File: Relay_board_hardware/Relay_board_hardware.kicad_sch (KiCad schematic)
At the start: 18 parts, among them IC1 BTS3800SL, Q1 IRF740ASPBF, U1 AD8541, U2 MCP1416

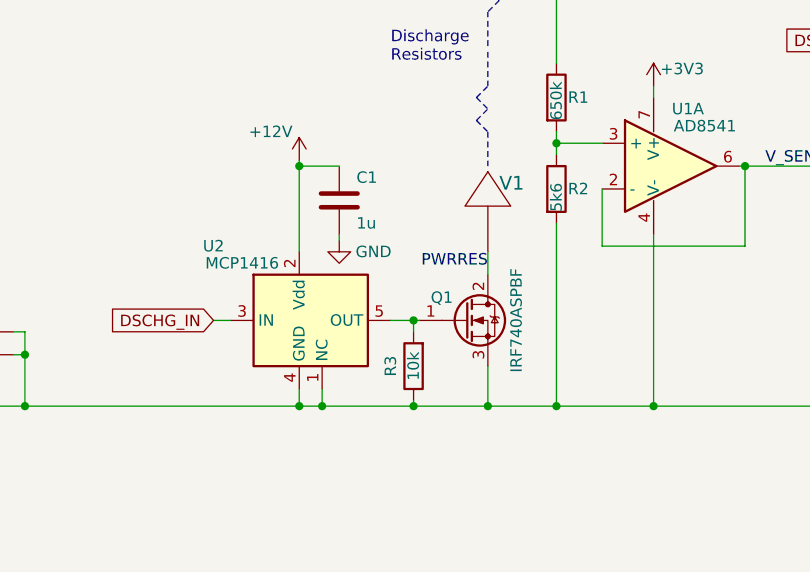
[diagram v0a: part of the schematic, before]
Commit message: added filter cap, changed opamp datasheet
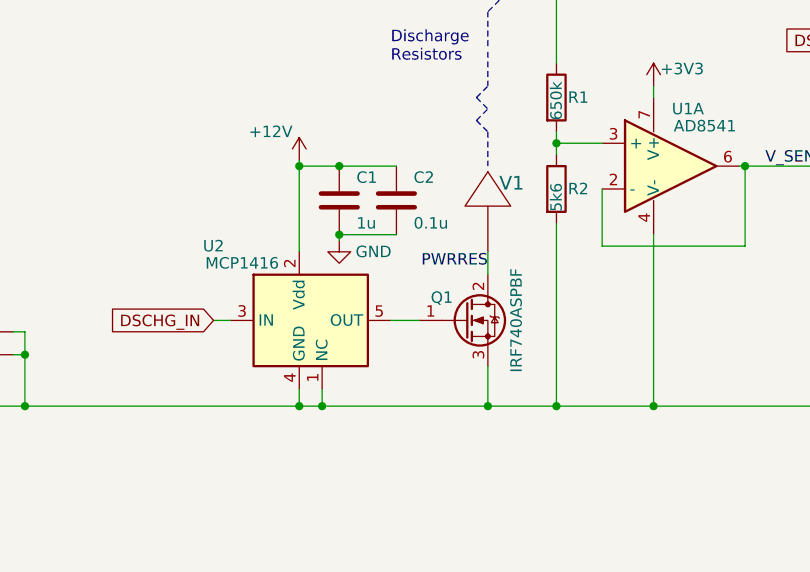
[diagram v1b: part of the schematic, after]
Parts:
- removed R3: 10k, Resistor_SMD:R_0603_1608Metric_Pad0.98x0.95mm_HandSolder, symbol Device:R
- added C2: 0.1u, Capacitor_SMD:C_0603_1608Metric_Pad1.08x0.95mm_HandSolder, symbol Device:C
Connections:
- net +12V: now also C2.1
- net GND: now also C2.2
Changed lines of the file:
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@@
   (junction (at 114.935 83.82) (diameter 0) (color 0 0 0 0)
   )
-  (junction (at 158.115 80.01) (diameter 0) (color 0 0 0 0)
-  )
   (junction (at 145.415 62.865) (diameter 0) (color 0 0 0 0)
   )
@@
   (junction (at 61.595 89.535) (diameter 0) (color 0 0 0 0)
   )
-  (junction (at 158.115 89.535) (diameter 0) (color 0 0 0 0)
-  )
   (junction (at 33.655 89.535) (diameter 0) (color 0 0 0 0)
   )
   (junction (at 184.785 89.535) (diameter 0) (color 0 0 0 0)
   )
+  (junction (at 149.86 70.485) (diameter 0) (color 0 0 0 0)
+  )
   (junction (at 114.935 89.535) (diameter 0) (color 0 0 0 0)
   )
@@
   (junction (at 147.955 89.535) (diameter 0) (color 0 0 0 0)
   )
+  (junction (at 149.86 62.865) (diameter 0) (color 0 0 0 0)
+  )
   (junction (at 46.355 54.61) (diameter 0) (color 0 0 0 0)
   )
@@
     (stroke (width 0) (type dash_dot))
   )
-  (wire (pts (xy 158.115 89.535) (xy 166.37 89.535))
-    (stroke (width 0) (type default))
-  )
   (wire (pts (xy 173.99 61.595) (xy 173.99 60.325))
     (stroke (width 0) (type default))
@@
     (stroke (width 0) (type default))
   )
-  (wire (pts (xy 158.115 88.9) (xy 158.115 89.535))
-    (stroke (width 0) (type default))
-  )
   (wire (pts (xy 179.07 71.755) (xy 194.945 71.755))
     (stroke (width 0) (type default))
   )
-  (wire (pts (xy 158.115 80.01) (xy 158.75 80.01))
-    (stroke (width 0) (type default))
-  )
   (wire (pts (xy 210.82 89.535) (xy 184.785 89.535))
     (stroke (width 0) (type default))
@@
     (stroke (width 0) (type default))
   )
-  (wire (pts (xy 158.115 80.01) (xy 158.115 81.28))
-    (stroke (width 0) (type default))
-  )
   (wire (pts (xy 38.735 57.785) (xy 38.735 44.45))
     (stroke (width 0) (type default))
@@
     (stroke (width 0) (type default))
   )
-  (wire (pts (xy 147.955 89.535) (xy 158.115 89.535))
+  (wire (pts (xy 147.955 89.535) (xy 166.37 89.535))
     (stroke (width 0) (type default))
   )
@@
     (stroke (width 0) (type default))
   )
+  (wire (pts (xy 149.86 70.485) (xy 156.21 70.485))
+    (stroke (width 0) (type default))
+  )
   (wire (pts (xy 114.935 83.82) (xy 114.935 81.28))
     (stroke (width 0) (type default))
   )
+  (wire (pts (xy 149.86 62.865) (xy 156.21 62.865))
+    (stroke (width 0) (type default))
+  )
   (wire (pts (xy 212.09 46.355) (xy 210.82 46.355))
     (stroke (width 0) (type default))
@@
     (stroke (width 0) (type default))
   )
-  (wire (pts (xy 155.575 80.01) (xy 158.115 80.01))
+  (wire (pts (xy 155.575 80.01) (xy 158.75 80.01))
     (stroke (width 0) (type default))
   )
@@
       (effects (font (size 1.27 1.27)) hide)
     )
-    (property "Datasheet" "https://www.mouser.com/ProductDetail/Microchip-Technology/MCP6497T-E-SN?qs=8Wlm6%252BaMh8Sq3ZIB9JIi0Q%3D%3D" (at 187.325 62.865 0)
+    (property "Datasheet" "https://www.digikey.com/en/products/detail/analog-devices-inc/AD8541ARZ-REEL7/996008" (at 187.325 62.865 0)
       (effects (font (size 1.27 1.27)) hide)
     )
@@
     )
   )
+  (symbol (lib_id "Device:C") (at 156.21 66.675 0) (unit 1)
+    (in_bom yes) (on_board yes) (dnp no)
+    (property "Reference" "C2" (at 158.115 64.135 0)
+      (effects (font (size 1.27 1.27)) (justify left))
+    )
+    (property "Value" "0.1u" (at 158.115 69.215 0)
+      (effects (font (size 1.27 1.27)) (justify left))
+    )
+    (property "Footprint" "Capacitor_SMD:C_0603_1608Metric_Pad1.08x0.95mm_HandSolder" (at 157.1752 70.485 0)
+      (effects (font (size 1.27 1.27)) hide)
+    )
+    (property "Datasheet" "~https://www.digikey.com/en/products/detail/yageo/CC1210KKX7R7BB105/7164418" (at 156.21 66.675 0)
+      (effects (font (size 1.27 1.27)) hide)
+    )
+    (pin "1")
+    (pin "2")
+    (instances
+      (project "Relay_board_hardware"
+        (path "/e63e39d7-6ac0-4ffd-8aa3-1841a4541b55"
+          (reference "C2") (unit 1)
+        )
+      )
+    )
+  )
   (symbol (lib_id "Device:Opamp_Dual") (at 186.69 62.865 0) (unit 1)
     (in_bom yes) (on_board yes) (dnp no)
@@
       (effects (font (size 1.27 1.27)) hide)
     )
-    (property "Datasheet" "https://www.mouser.com/ProductDetail/Microchip-Technology/MCP6497T-E-SN?qs=8Wlm6%252BaMh8Sq3ZIB9JIi0Q%3D%3D" (at 186.69 62.865 0)
+    (property "Datasheet" "https://www.digikey.com/en/products/detail/analog-devices-inc/AD8541ARZ-REEL7/996008" (at 186.69 62.865 0)
       (effects (font (size 1.27 1.27)) hide)
     )
@@
         )
       )
-    )
-  )
-  (symbol (lib_id "Device:R") (at 158.115 85.09 180) (unit 1)
-    (in_bom yes) (on_board yes) (dnp no)
-    (property "Reference" "R3" (at 155.575 85.09 90)
-      (effects (font (size 1.27 1.27)))
-    )
-    (property "Value" "10k" (at 158.115 85.09 90)
-      (effects (font (size 1.27 1.27)))
-    )
-    (property "Footprint" "Resistor_SMD:R_0603_1608Metric_Pad0.98x0.95mm_HandSolder" (at 159.893 85.09 90)
-      (effects (font (size 1.27 1.27)) hide)
-    )
-    (property "Datasheet" "https://www.mouser.com/ProductDetail/Vishay-Dale/CRCW2512649KFKEG?qs=WpL82mpZNv9YmPWivNEPLA%3D%3D" (at 158.115 85.09 0)
-      (effects (font (size 1.27 1.27)) hide)
-    )
-    (property "Price" "0.37" (at 158.115 85.09 0)
-      (effects (font (size 1.27 1.27)) hide)
-    )
-    (pin "1")
-    (pin "2")
-    (instances
-      (project "Relay_board_hardware"
-        (path "/e63e39d7-6ac0-4ffd-8aa3-1841a4541b55"
-          (reference "R3") (unit 1)
-        )
-      )
